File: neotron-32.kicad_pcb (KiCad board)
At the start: 4 copper layers, 166.9 x 140.7 mm, 97 parts, among them J1 Conn_02x06, J10 micro SD Card, J11 Conn_02x13_Top_Bottom, J12 AVR-ISP-6, J13 DE9 Male, J14 DE9 Male, J15 Double-mini-DIN-6, J17 DB15HD_Female, J18 Conn_02x05, J2 Conn_02x06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

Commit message: Join VGA GND together.
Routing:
- net GND: track 1.46 -> 6.04 mm
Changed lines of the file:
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@@
     (thickness 1.6)
     (drawings 49)
-    (tracks 1040)
+    (tracks 1041)
     (zones 0)
     (modules 97)
@@
   )
   (setup
-    (last_trace_width 1.016)
+    (last_trace_width 0.254)
     (user_trace_width 0.254)
     (user_trace_width 0.508)
@@
   (segment (start 232.851 136.905) (end 231.395 136.905) (width 0.254) (layer F.Cu) (net 1) (status 10))
   (via (at 231.14 136.905) (size 1.016) (drill 0.635) (layers F.Cu B.Cu) (net 1))
+  (segment (start 82.62 116.015) (end 82.62 120.595) (width 0.508) (layer Gnd.Cu) (net 1))
   (segment (start 105.41 27.94) (end 107.95 25.4) (width 1.016) (layer Vcc.Cu) (net 2) (status 20))
   (segment (start 101.6 27.94) (end 105.41 27.94) (width 1.016) (layer Vcc.Cu) (net 2) (status 10))

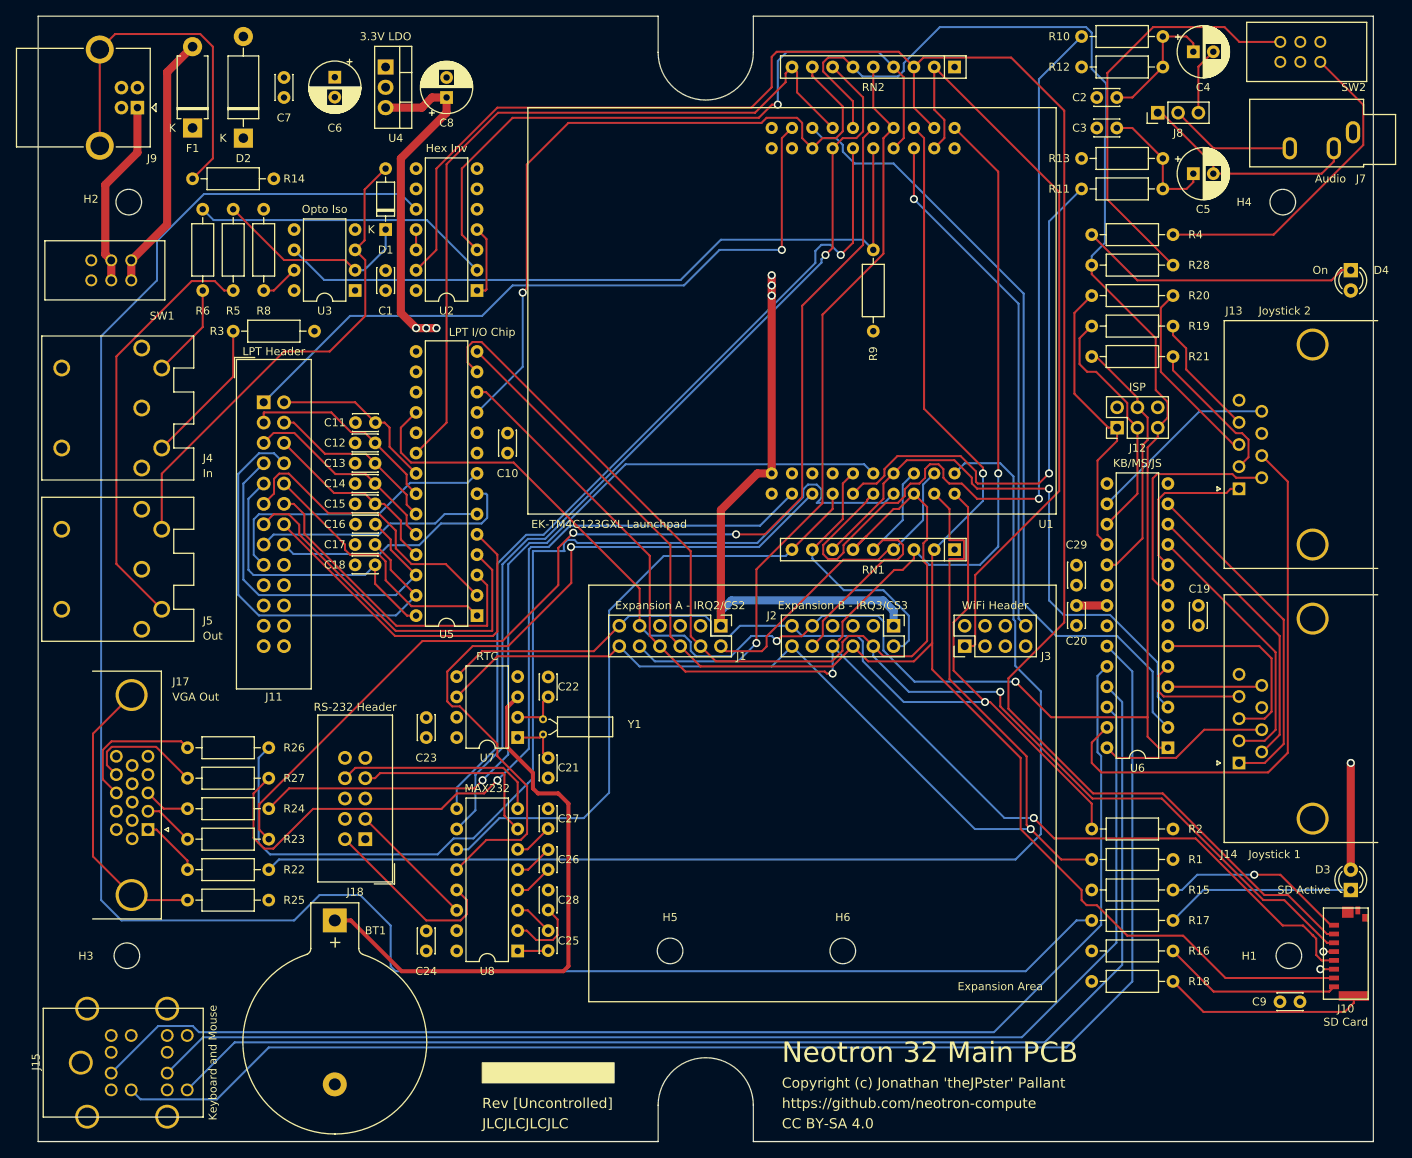
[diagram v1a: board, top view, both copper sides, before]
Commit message: Manhattan, not diagonals.
Aligning tracks on north/south and east/west is more
visually pleasing than taking the diagonal. Having to fight the autorouter
a bit though. In an ideal work we'd have north/south on one layer
and east/west on the other, but meh.
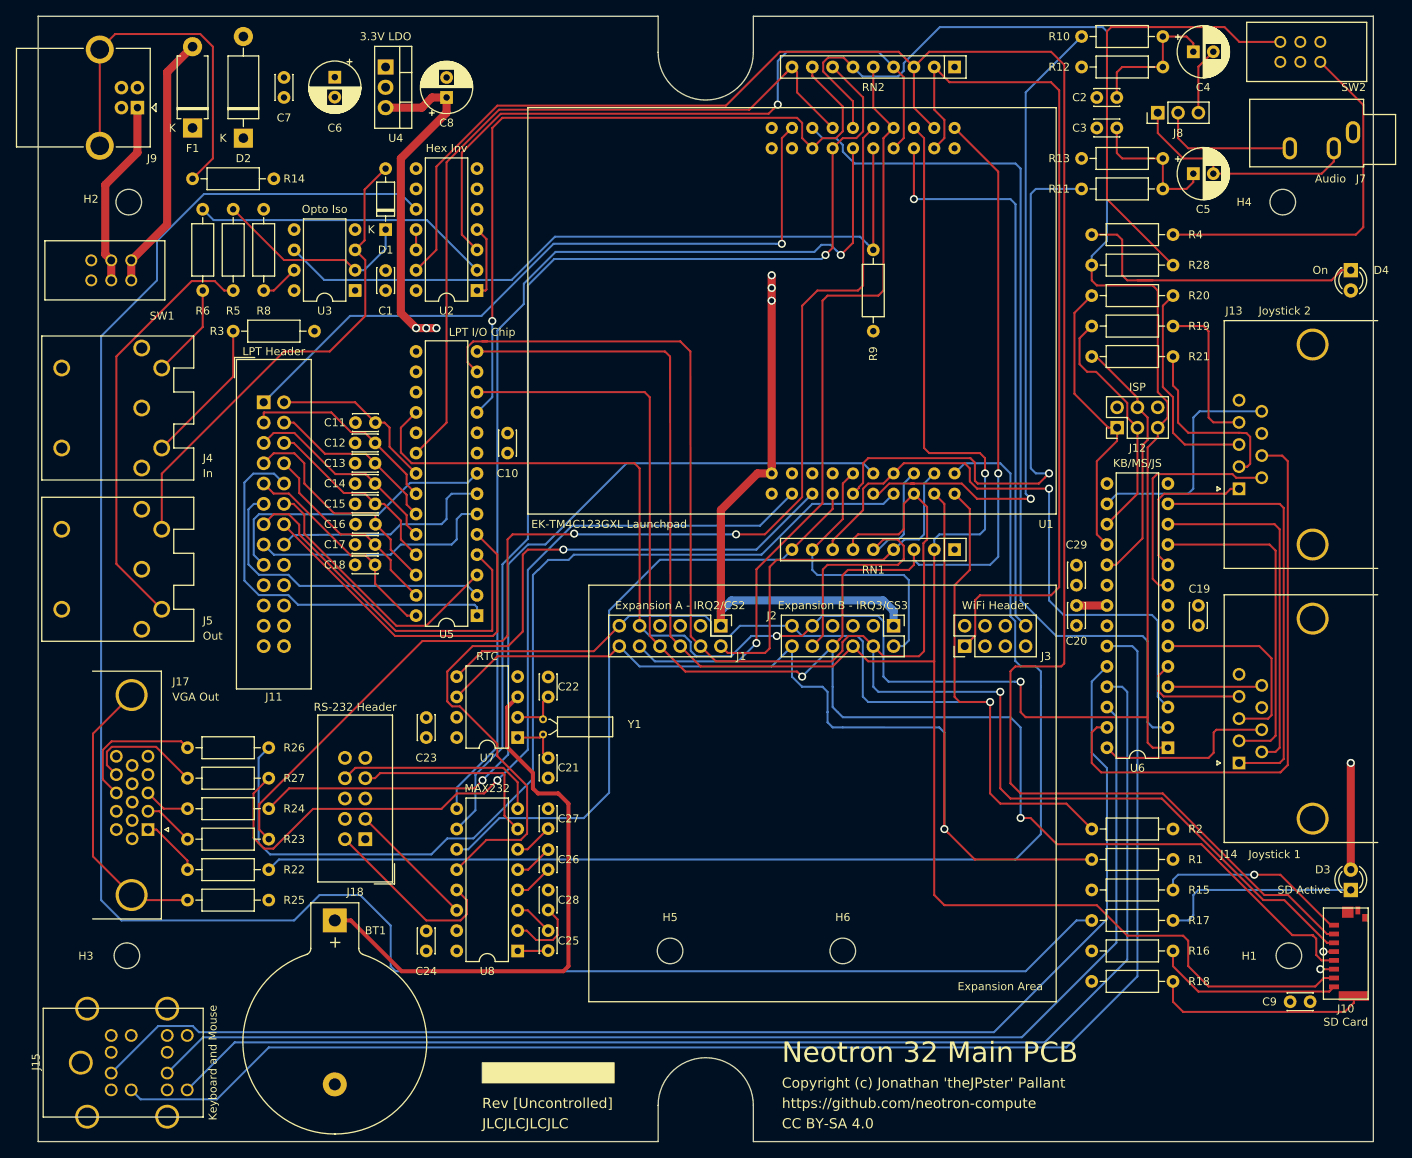
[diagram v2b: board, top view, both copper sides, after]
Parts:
- moved C9 1.27 mm to (227.4, 141.0)
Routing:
- net /PA4_SPI_MISO: track 228.7 -> 261.6 mm
- net /Parallel Printer/D6: track 55.2 -> 25.1 mm
- net /PA2_SPI_CLK: track 232.6 -> 259.0 mm
- net /PE5_AUDIO_R: track 106.4 -> 82.4 mm
- net /PA5_SPI_MOSI: track 195.4 -> 218.9 mm
- net /Parallel Printer/D5: track 47.5 -> 28.8 mm
- net /PC4_U1RTS: track 120.1 -> 138.4 mm
- net /~RESET: track 268.6 -> 286.8 mm
- net /PC5_U1CTS: track 107.5 -> 125.2 mm
- net /Parallel Printer/ACK: track 32.7 -> 49.7 mm
- net /PD7_U2TX: track 95.6 -> 107.6 mm
- net /PE0_U7RX: track 101.6 -> 113.6 mm
- net /~PA3_SPI_CS0: track 243.2 -> 253.6 mm
- net /Parallel Printer/D7: track 37.3 -> 27.3 mm
- net /PA7_I2C_SDA: track 128.1 -> 138.1 mm
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
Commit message: Swapped WiFi pin header for socket. Removed 5V from 3.3V plane.
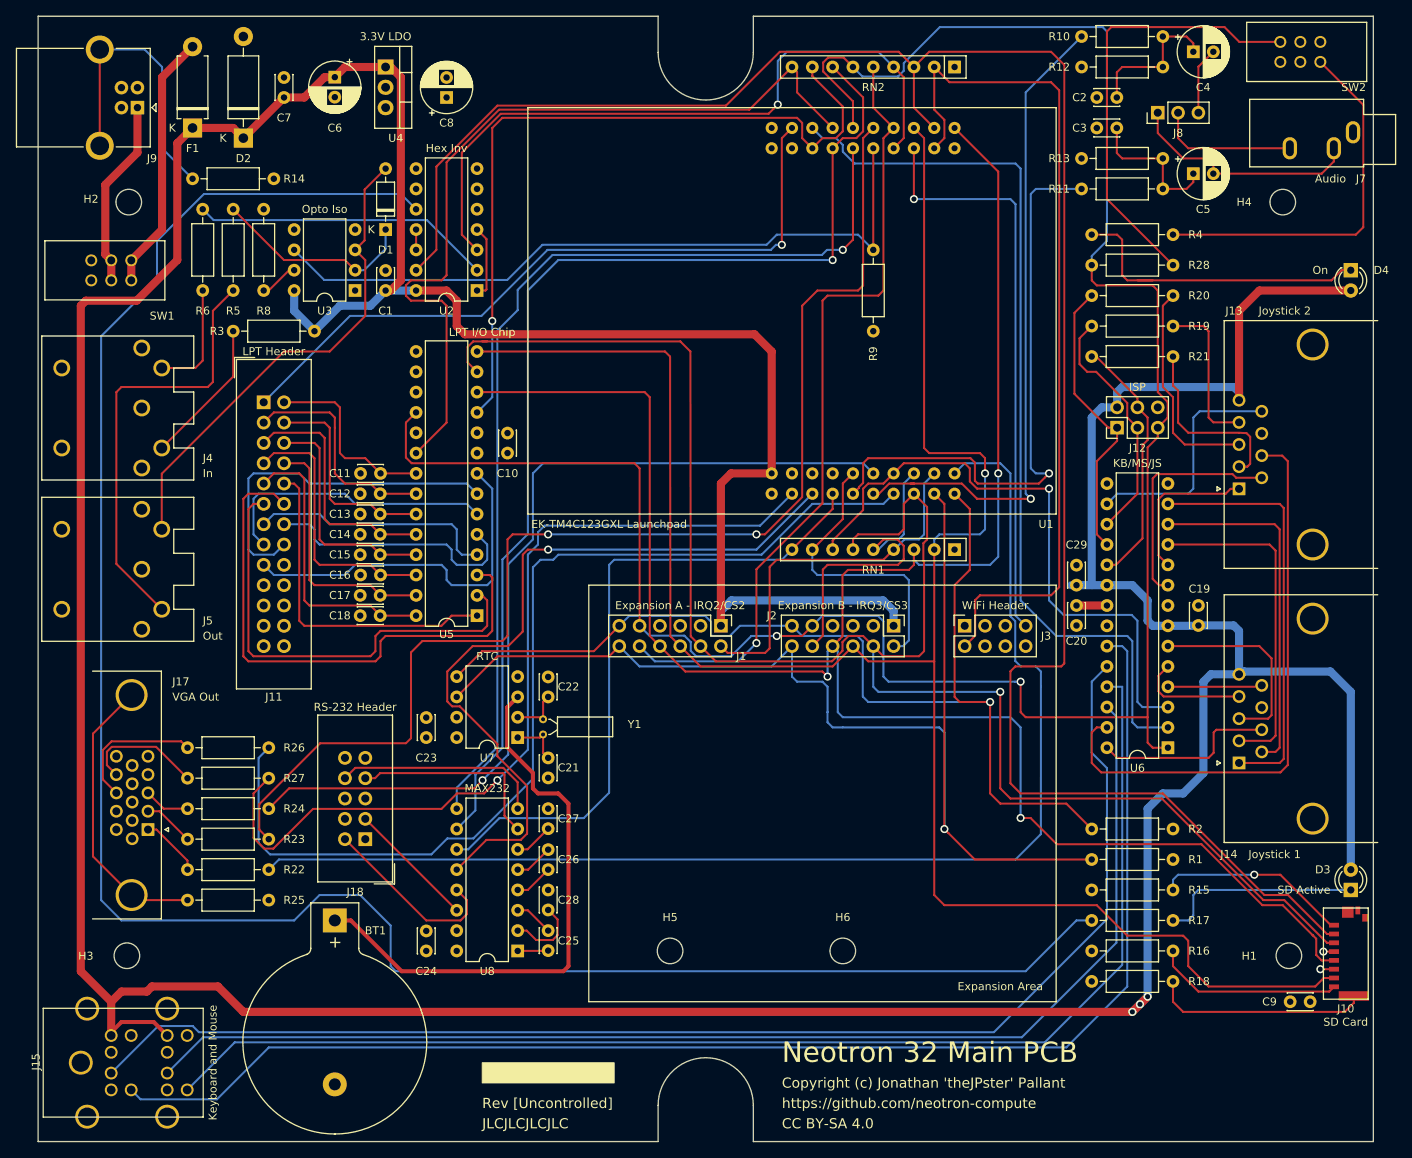
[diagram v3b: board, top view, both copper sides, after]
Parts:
- J3: footprint Connector_PinHeader_2.54mm:PinHeader_2x04_P2.54mm_Vertical -> Connector_PinSocket_2.54mm:PinSocket_2x04_P2.54mm_Vertical
- moved C11 6.38 mm to (111.2, 74.9)
- moved C13 6.38 mm to (111.1, 80.0)
- moved C15 6.38 mm to (111.1, 85.1)
- moved C17 6.38 mm to (111.1, 90.2)
- moved C12 6.38 mm to (111.1, 77.5)
- moved C14 6.38 mm to (111.1, 82.5)
- moved C16 6.38 mm to (111.2, 87.6)
- moved C18 6.38 mm to (111.1, 92.7)
- moved J3 2.54 mm to (186.7, 94.0)
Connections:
- J3 pad 1: /PD7_U2TX -> +3V3
- J3 pad 2: +3V3 -> /PD7_U2TX
- J3 pad 7: GND -> /PD6_U2RX
- J3 pad 8: /PD6_U2RX -> GND
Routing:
- net +5V: track 115.6 -> 649.4 mm, vias 4 -> 3
- net +3V3: track 44.1 -> 1.41 mm, vias 4 -> 1
- net /Parallel Printer/POUT: track 35.1 -> 69.0 mm
- net /Parallel Printer/~BUSY: track 39.2 -> 57.5 mm
- net /Parallel Printer/RESET: track 28.2 -> 44.0 mm
- net /Parallel Printer/SELECT: track 46.2 -> 30.8 mm
- net /Parallel Printer/~LF: track 45.9 -> 33.0 mm
- net /Parallel Printer/~SELPRI: track 36.5 -> 45.8 mm
- net Net-(J9-Pad5): track 45.2 -> 36.3 mm
- net /~PF0_IRQ1: track 95.8 -> 104.4 mm
- net /Parallel Printer/D7: track 27.3 -> 35.9 mm
- net /Parallel Printer/ACK: track 49.7 -> 41.7 mm
- net /Parallel Printer/D6: track 25.1 -> 31.6 mm
- net /PB7_VGA_GREEN: track 148.6 -> 154.8 mm
- net /Parallel Printer/D4: track 23.7 -> 29.0 mm
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- removed copper zone on Vcc.Cu, net +5V

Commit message: More de-diagonalisation.
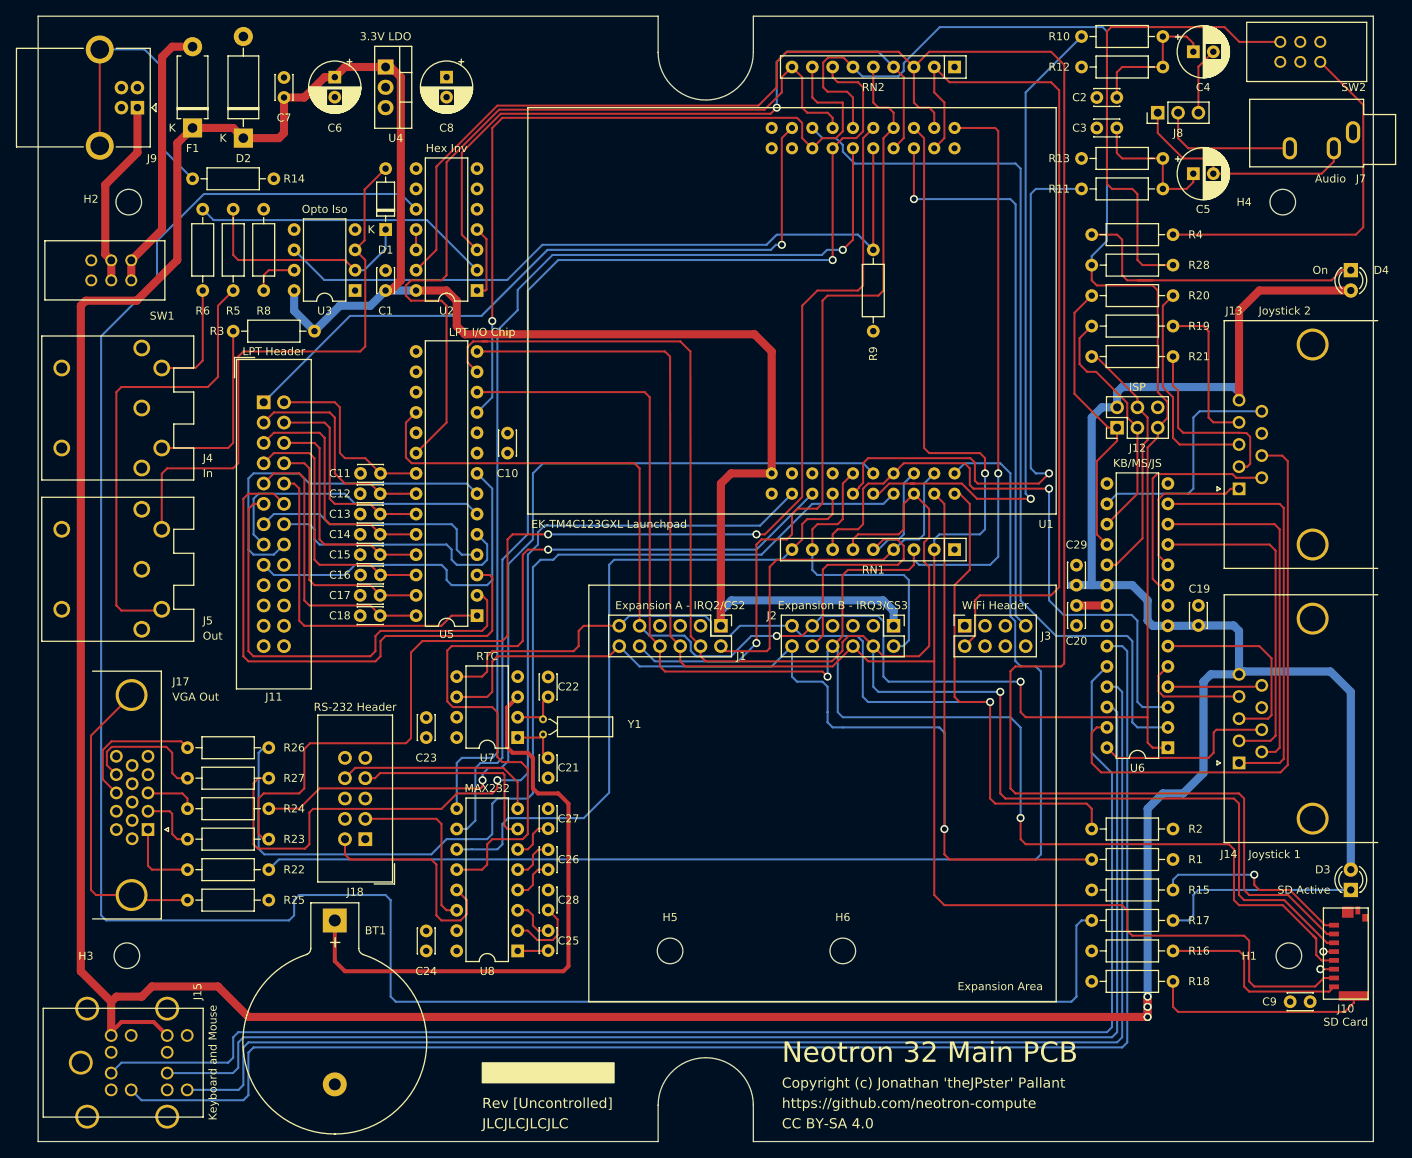
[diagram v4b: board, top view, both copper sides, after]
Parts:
- moved C8 2.54 mm to (121.9, 25.4), turned to 270 degrees
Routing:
- net Net-(R17-Pad2): track 256.6 -> 271.3 mm
- net /PA2_SPI_CLK: track 260.9 -> 271.1 mm
- net Net-(D1-Pad2): track 61.1 -> 71.1 mm
- net /~PA3_SPI_CS0: track 253.6 -> 263.2 mm
- net /Keyboard, Mouse and Joystick/KB_DAT: track 166.2 -> 175.9 mm
- net /PA5_SPI_MOSI: track 218.9 -> 227.4 mm
- net /Keyboard, Mouse and Joystick/MS_DAT: track 155.3 -> 163.6 mm
- net /Keyboard, Mouse and Joystick/MS_CLK: track 160.0 -> 167.7 mm
- net /PB0_U1RX: track 96.1 -> 103.7 mm
- net /Keyboard, Mouse and Joystick/KB_CLK: track 175.6 -> 182.9 mm
- net /RS-232 Serial Port/RS232_TX_OUT: track 16.2 -> 22.1 mm
- net /PB5_VGA_VSYNC: track 109.7 -> 115.5 mm
- net Net-(J4-Pad4): track 18.3 -> 23.2 mm
- net /RS-232 Serial Port/RS232_RX_IN: track 23.3 -> 28.2 mm
- net +5V: track 649.4 -> 653.8 mm
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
